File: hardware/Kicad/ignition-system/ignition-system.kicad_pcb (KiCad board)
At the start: 2 copper layers, 92 x 60.2 mm, 27 parts, among them J1 Screw_Terminal_01x02, SW1 SW_Push, SW2 SW_SPDT

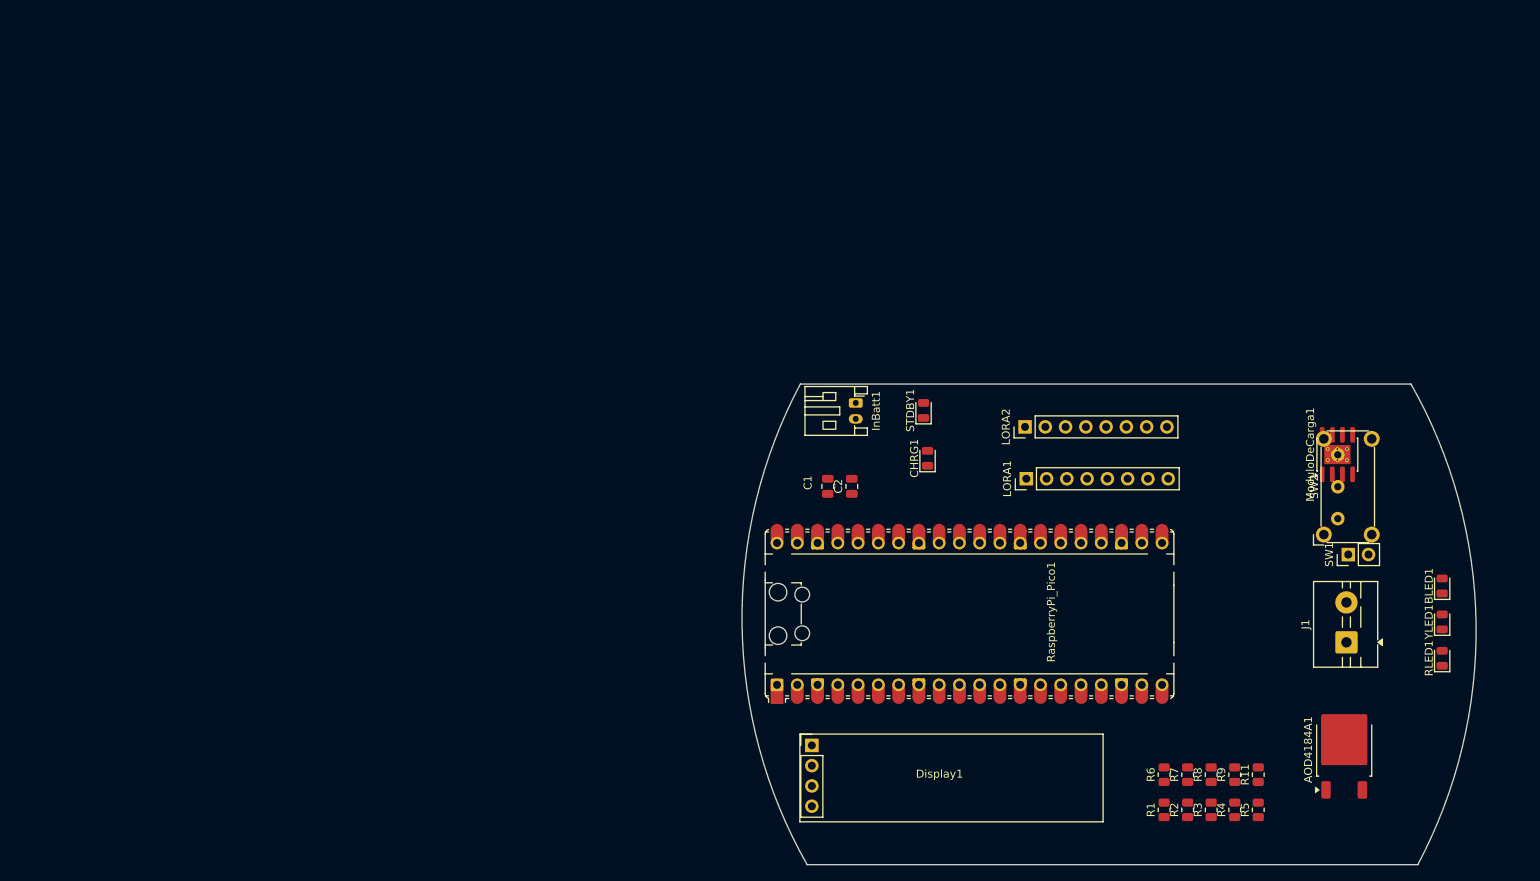
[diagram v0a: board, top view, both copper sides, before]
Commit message: feat: net class power, contorno 70x50 y placement completo
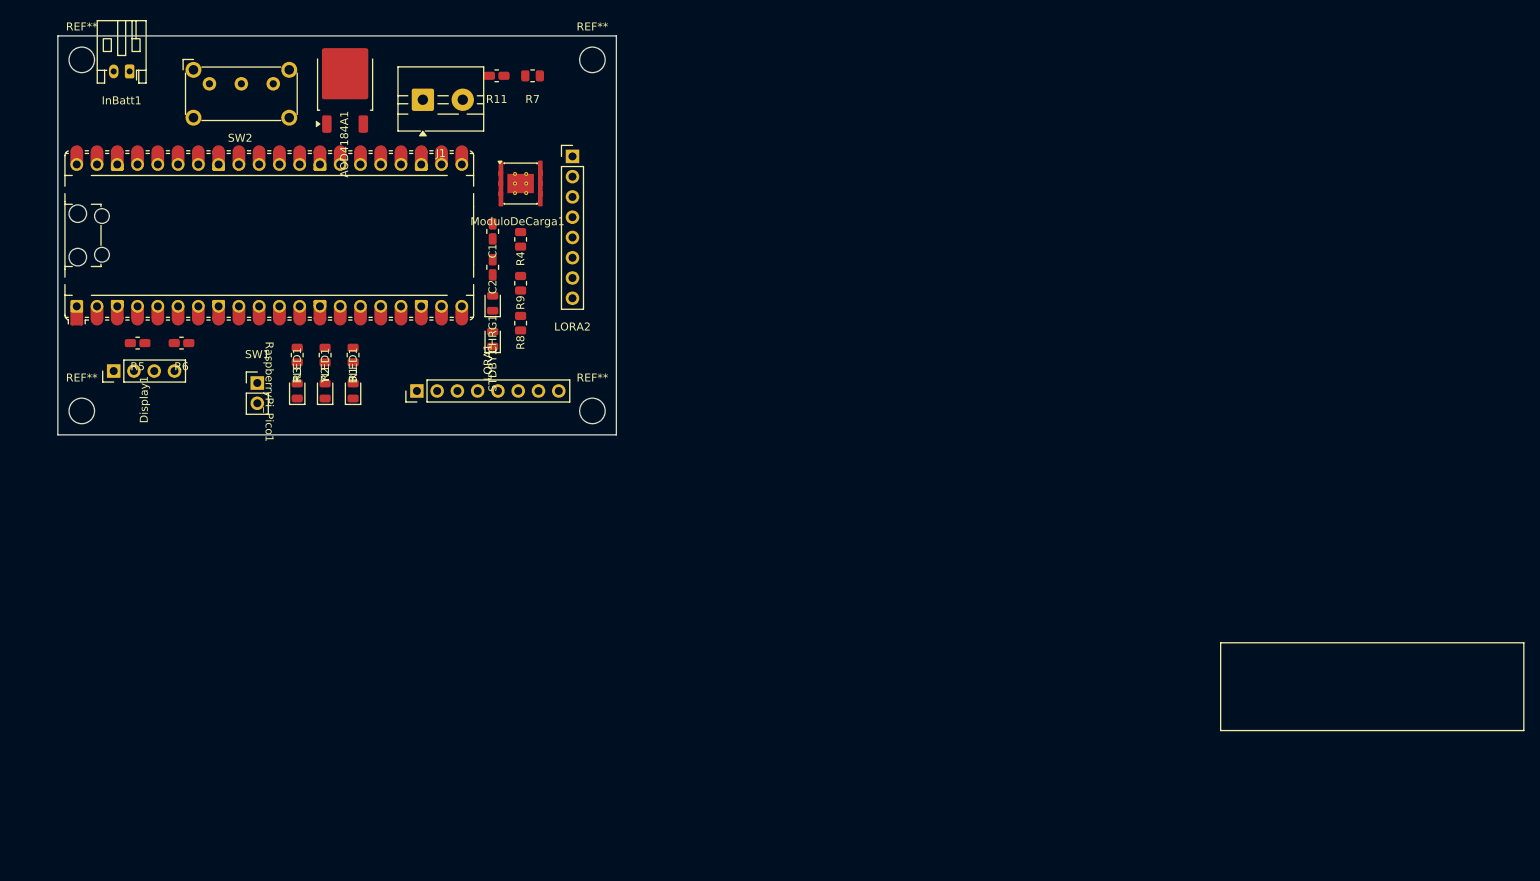
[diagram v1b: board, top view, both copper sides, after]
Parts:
- added REF**: MountingHole_3.2mm_M3, MountingHole:MountingHole_3.2mm_M3, F.Cu at (34.0, 33.0)
- added REF**: MountingHole_3.2mm_M3, MountingHole:MountingHole_3.2mm_M3, F.Cu at (98.0, 33.0)
- added REF**: MountingHole_3.2mm_M3, MountingHole:MountingHole_3.2mm_M3, F.Cu at (98.0, 77.0)
- added REF**: MountingHole_3.2mm_M3, MountingHole:MountingHole_3.2mm_M3, F.Cu at (34.0, 77.0)
- moved R5 152.1 mm to (41.0, 68.5), turned to 0 degrees
- moved SW2 151.6 mm to (50.0, 36.0), turned to 0 degrees
- moved AOD4184A1 150.5 mm to (67.0, 36.0)
- moved RLED1 147.4 mm to (61.0, 74.5)
- moved YLED1 143.0 mm to (64.5, 74.5)
- moved BLED1 138.7 mm to (68.0, 74.5)
- moved SW1 138.4 mm to (56.0, 73.5), turned to 0 degrees
- moved R6 134.5 mm to (46.5, 68.5), turned to 0 degrees
- moved J1 134.2 mm to (76.8, 38.0), turned to 0 degrees
- moved R11 129.5 mm to (86.0, 35.0), turned to 0 degrees
- moved R3 127.9 mm to (61.0, 70.0)
- moved R2 122.2 mm to (64.5, 70.0)
- moved R7 120.0 mm to (90.5, 35.0), turned to 0 degrees
- moved R1 116.5 mm to (68.0, 70.0)
- moved R4 114.6 mm to (89.0, 55.5)
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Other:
- board size 92 x 60.2 mm -> 70 x 50 mm

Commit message: fix: socket ra02 con gnd de bordes y ntc al temp
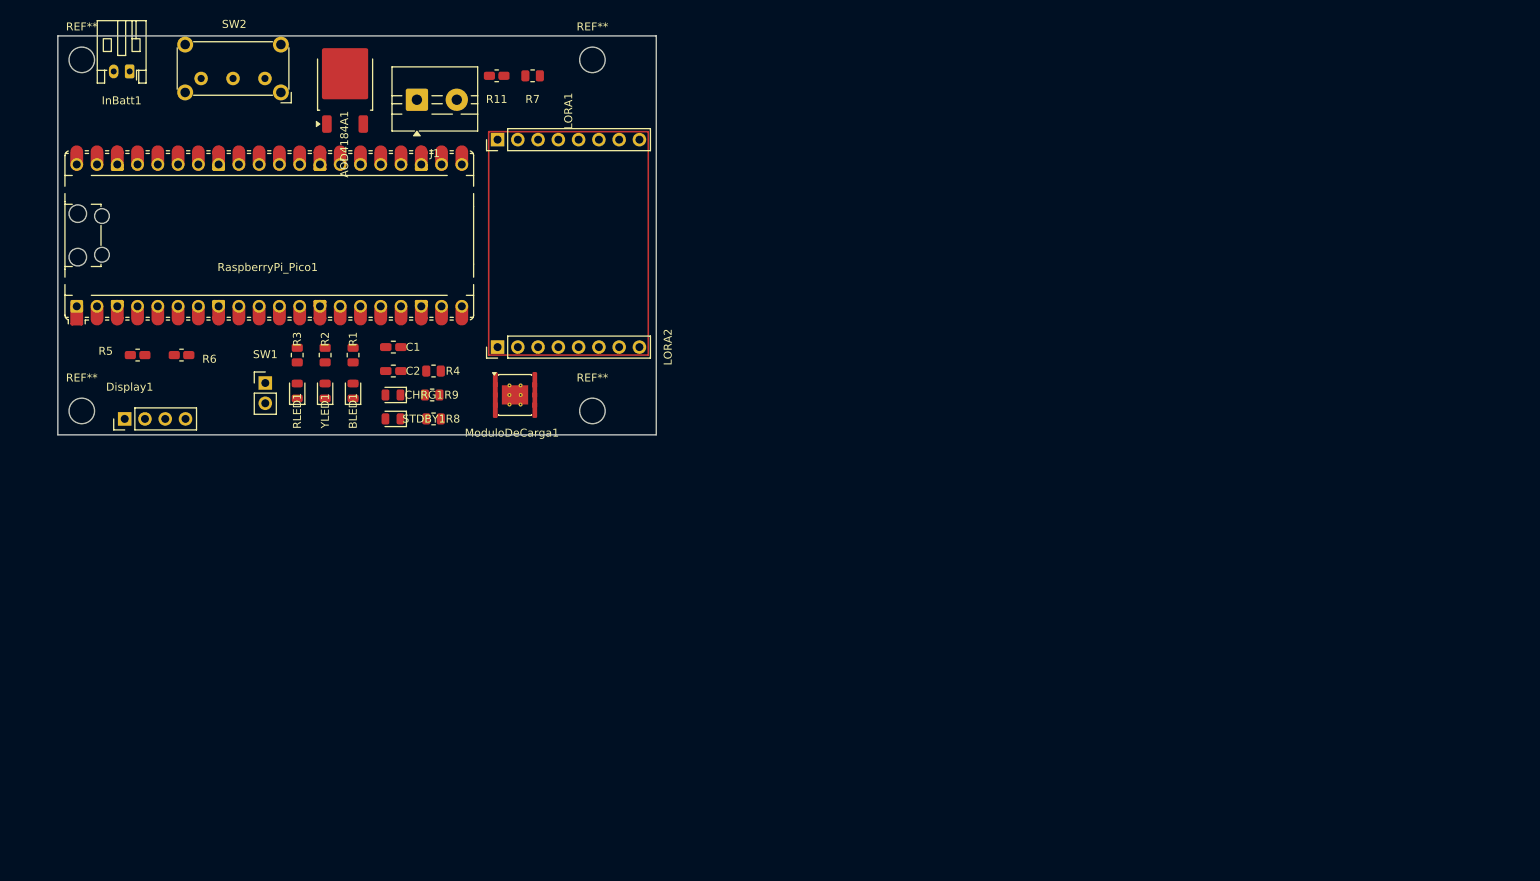
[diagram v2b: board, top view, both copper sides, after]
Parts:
- moved LORA1 33.1 mm to (86.1, 43.0)
- moved ModuloDeCarga1 26.5 mm to (88.3, 75.0)
- moved LORA2 25.7 mm to (86.1, 69.0), turned to 90 degrees
- moved R4 19.8 mm to (78.1, 72.0), turned to 180 degrees
- moved C1 19.1 mm to (73.0, 69.0), turned to 180 degrees
- moved C2 18.0 mm to (73.0, 72.0), turned to 180 degrees
- moved R9 17.9 mm to (77.9, 75.0), turned to 180 degrees
- moved CHRG1 17.0 mm to (73.0, 75.0), turned to 180 degrees
- moved R8 16.2 mm to (78.1, 78.0), turned to 180 degrees
- moved STDBY1 16.0 mm to (73.0, 78.0), turned to 180 degrees
- moved SW2 6.99 mm to (57.0, 35.3), turned to 180 degrees
- moved Display1 6.16 mm to (39.4, 78.0)
- moved R5 1.50 mm to (41.0, 70.0)
- moved R6 1.50 mm to (46.5, 70.0)
- moved SW1 1.00 mm to (57.0, 73.5)
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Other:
- board size 70 x 50 mm -> 75 x 50 mm

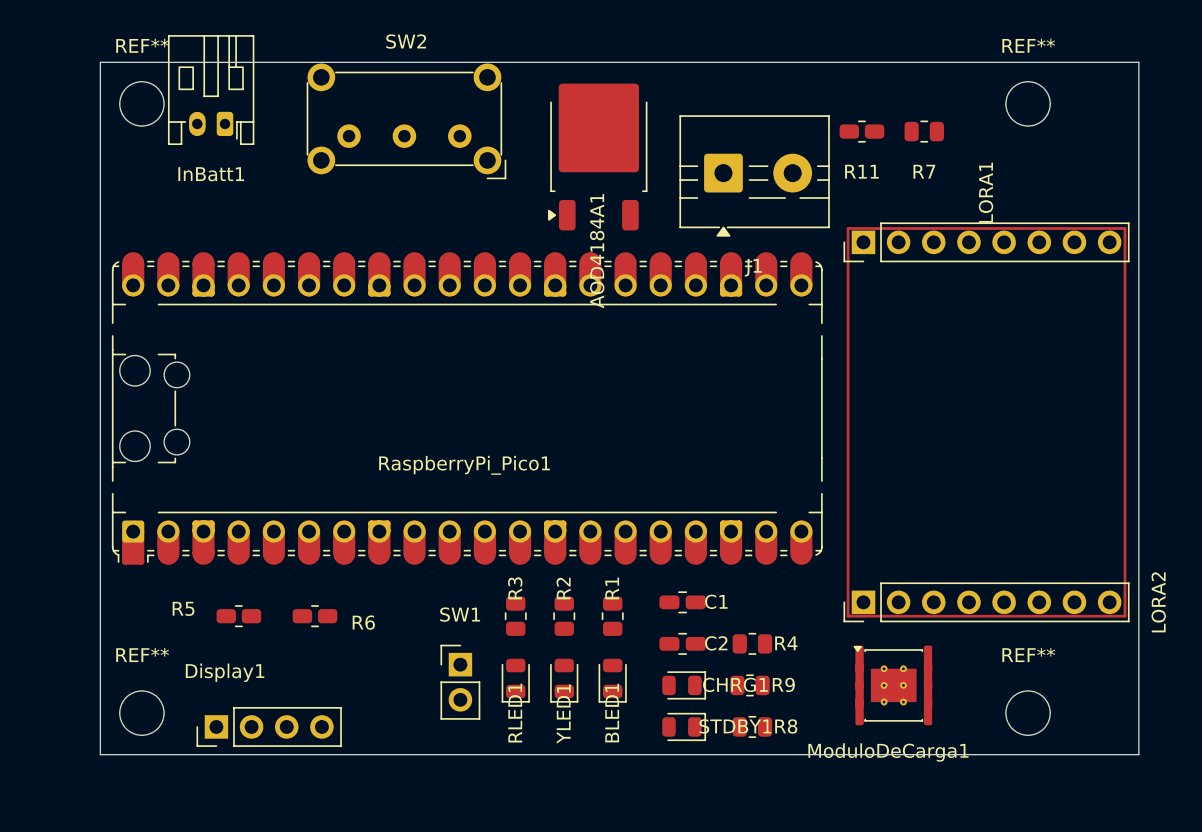
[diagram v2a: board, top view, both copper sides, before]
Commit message: feat: sw3 en consumo, tp4056 fijo a bateria, pwr flag de v
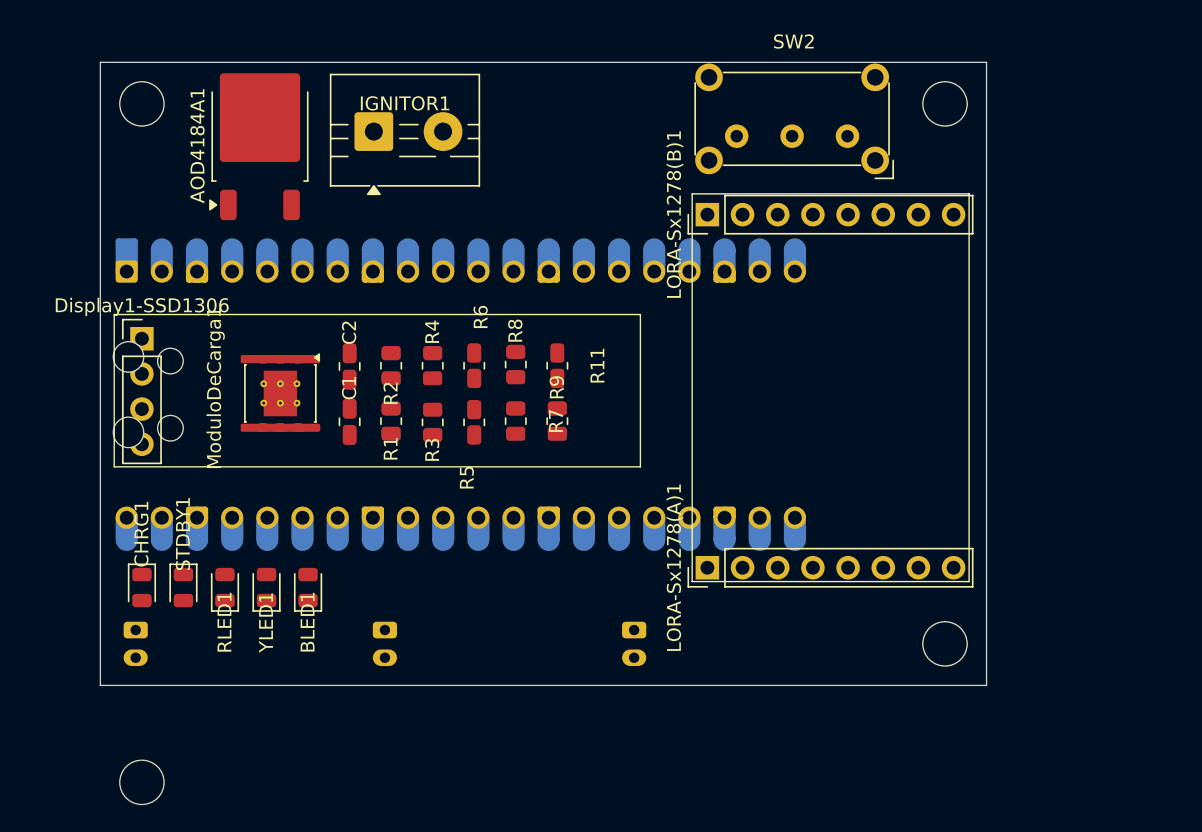
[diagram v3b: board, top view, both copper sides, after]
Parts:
- removed Display1: Conn_01x04, Connector_PinHeader_2.54mm:PinHeader_1x04_P2.54mm_Vertical
- removed J1: Screw_Terminal_01x02, TerminalBlock:TerminalBlock_MaiXu_MX126-5.0-02P_1x02_P5.00mm
- removed LORA1, LORA2: Conn_01x08, Connector_PinHeader_2.54mm:PinHeader_1x08_P2.54mm_Vertical
- removed RaspberryPi_Pico1: RaspberryPi_Pico, Module:RaspberryPi_Pico_Common_Unspecified
- added Display1-SSD1306: Conn_01x04, Connector_PinHeader_2.54mm:PinHeader_1x04_P2.54mm_Vertical, F.Cu at (34.0, 50.0)
- added IGNITOR1: Screw_Terminal_01x02, TerminalBlock:TerminalBlock_MaiXu_MX126-5.0-02P_1x02_P5.00mm, F.Cu at (50.8, 35.0)
- added LORA-Sx1278(A)1: Conn_01x08, Connector_PinHeader_2.54mm:PinHeader_1x08_P2.54mm_Vertical, F.Cu at (74.8, 66.5)
- added LORA-Sx1278(B)1: Conn_01x08, Connector_PinHeader_2.54mm:PinHeader_1x08_P2.54mm_Vertical, F.Cu at (74.8, 41.0)
- added RaspberryPi_Pico1-RP2040: RaspberryPi_Pico, Module:RaspberryPi_Pico_Common_Unspecified, B.Cu at (57.0, 54.0)
- added TH1: NTC 10k B3950, Connector_JST:JST_PH_S2B-PH-K_1x02_P2.00mm_Horizontal, B.Cu at (51.5, 71.0)
- InBatt1: moved to B.Cu
- SW1: footprint Connector_PinHeader_2.54mm:PinHeader_1x02_P2.54mm_Vertical -> Connector_JST:JST_PH_S2B-PH-K_1x02_P2.00mm_Horizontal; moved to B.Cu
- moved ModuloDeCarga1 49.1 mm to (44.0, 53.9), turned to -90 degrees
- moved CHRG1 39.6 mm to (34.0, 67.9), turned to -90 degrees
- moved STDBY1 37.4 mm to (37.0, 67.9), turned to -90 degrees
- moved InBatt1 37.1 mm to (33.5, 71.0), turned to -90 degrees
- moved R7 36.2 mm to (61.0, 55.9), turned to 90 degrees
- moved C2 31.3 mm to (49.0, 52.0), turned to -90 degrees
- moved R8 31.3 mm to (61.0, 51.8), turned to -90 degrees
- moved R4 30.6 mm to (55.0, 51.9), turned to -90 degrees
- moved SW2 28.0 mm to (85.0, 35.3)
- moved R11 27.7 mm to (64.0, 51.9), turned to 90 degrees
- moved C1 27.4 mm to (49.0, 56.0), turned to -90 degrees
- moved AOD4184A1 24.5 mm to (42.5, 35.3)
- moved R9 23.6 mm to (64.0, 55.9), turned to -90 degrees
- moved BLED1 23.0 mm to (46.0, 67.9)
- moved YLED1 22.5 mm to (43.0, 67.9)
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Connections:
- ModuloDeCarga1 pad 1: GND -> Net-(ModuloDeCarga1-TEMP)
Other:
- board size 75 x 50 mm -> 64 x 45 mm

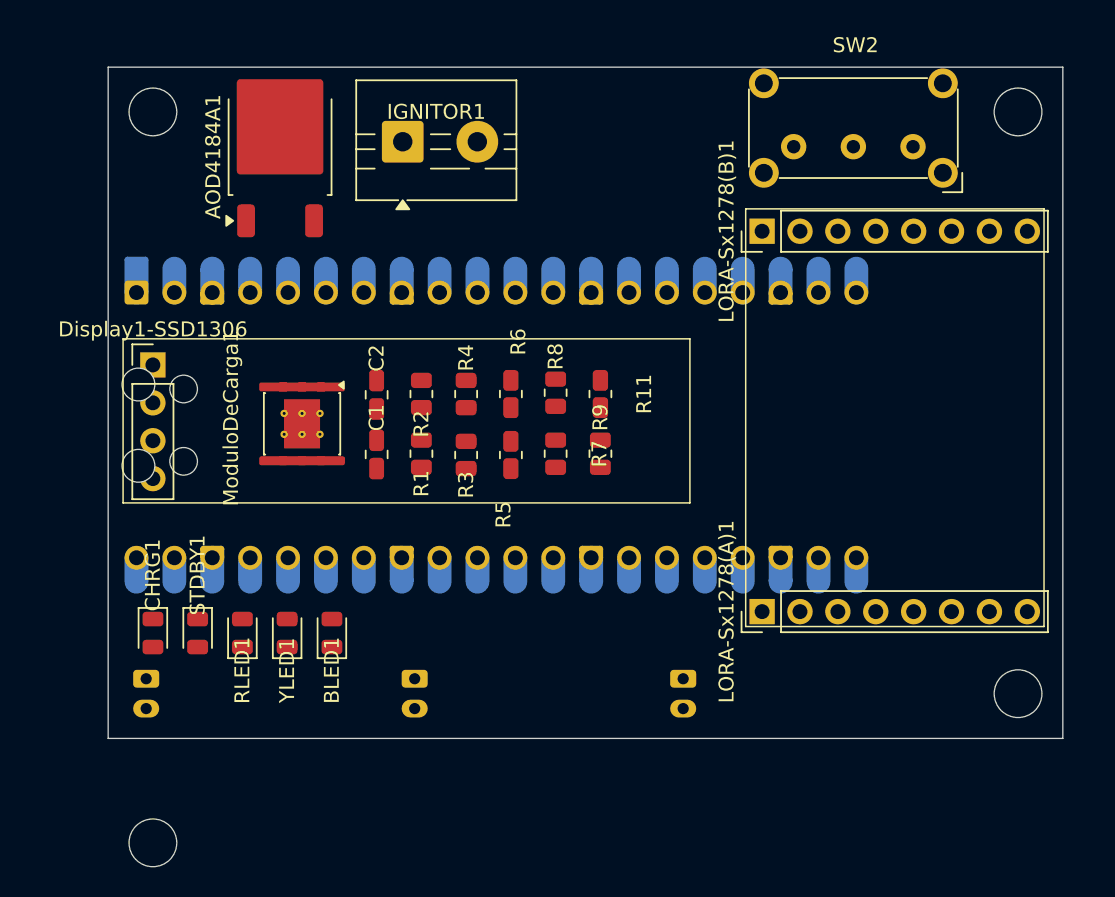
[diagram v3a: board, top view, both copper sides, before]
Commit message: feat: ruteo pcb de ignition-system
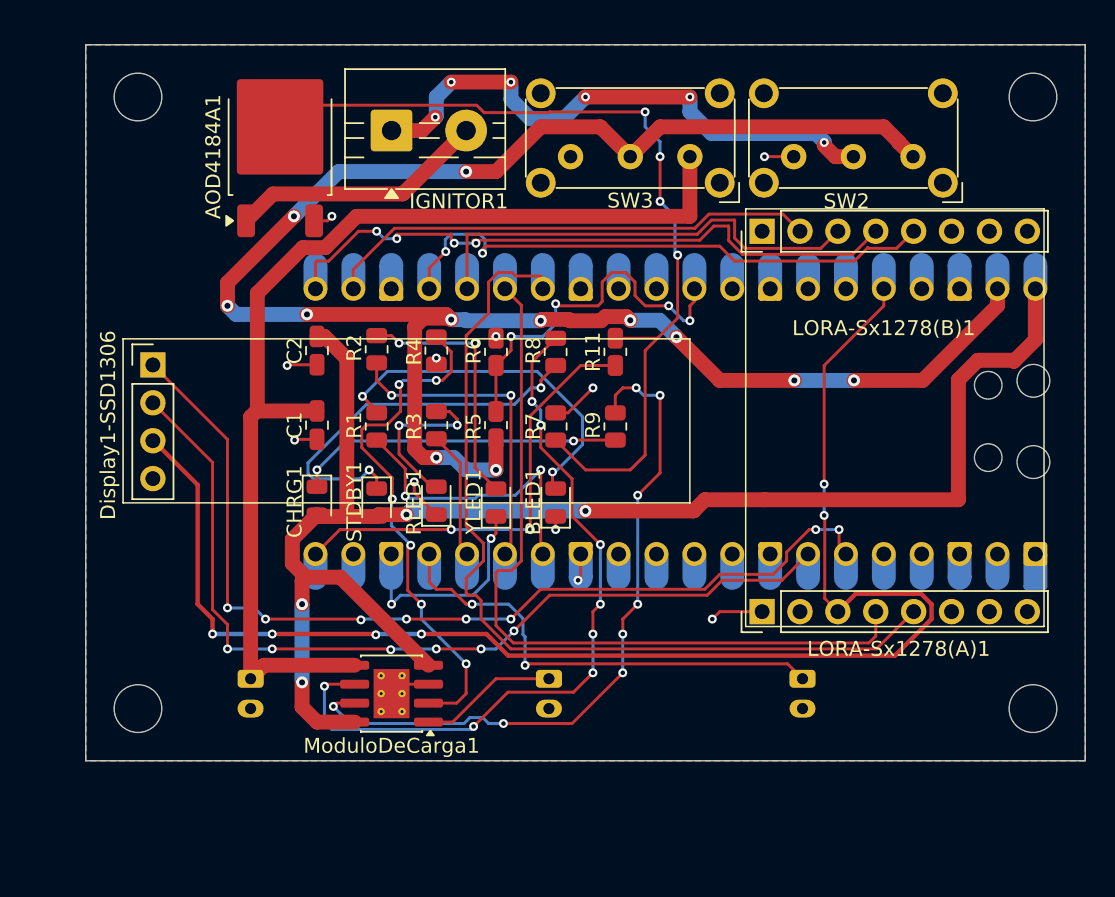
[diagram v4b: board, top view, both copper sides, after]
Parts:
- added SW3: SW_SPDT, Button_Switch_THT:SW_E-Switch_EG1224_SPDT_Angled, F.Cu at (70.0, 36.0)
- moved ModuloDeCarga1 19.1 mm to (50.0, 72.0), turned to 180 degrees
- moved BLED1 17.4 mm to (61.0, 59.2)
- moved YLED1 16.5 mm to (57.0, 59.2)
- moved RLED1 15.7 mm to (53.0, 59.1)
- moved STDBY1 14.9 mm to (49.0, 59.2)
- moved CHRG1 14.1 mm to (45.0, 59.1)
- moved RaspberryPi_Pico1-RP2040 12.0 mm to (69.0, 53.8), turned to 90 degrees
- moved REF** 9.06 mm to (33.0, 73.0)
- moved TH1 9.00 mm to (60.5, 71.0)
- moved SW1 8.00 mm to (77.5, 71.0)
- moved InBatt1 7.00 mm to (40.5, 71.0)
- moved C2 4.98 mm to (45.0, 49.0)
- moved C1 4.46 mm to (45.0, 54.0)
- moved R2 4.24 mm to (49.0, 48.9)
- moved R4 3.53 mm to (53.0, 49.0)
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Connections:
- C1 pad 1: VSYS -> Net-(InBatt1-Pin_1)
- InBatt1 pad 1: VSYS -> Net-(InBatt1-Pin_1)
- ModuloDeCarga1 pad 5: VSYS -> Net-(InBatt1-Pin_1)
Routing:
- net VSYS: track 0.00 -> 130.6 mm, vias 0 -> 12
- net VBUS: track 0.00 -> 103.1 mm, vias 0 -> 4
- net 3V3: track 0.00 -> 96.3 mm, vias 0 -> 6
- net Net-(InBatt1-Pin_1): track 0.00 -> 72.5 mm
- net SDA: track 0.00 -> 64.6 mm, vias 0 -> 8
- net DIO0: track 0.00 -> 60.5 mm
- net Net-(AOD4184A1-G): track 0.00 -> 60.2 mm, vias 0 -> 4
- net SCL: track 0.00 -> 60.2 mm, vias 0 -> 6
- net RST: track 0.00 -> 52.0 mm
- net STDBY: track 0.00 -> 49.5 mm, vias 0 -> 8
- net CHRG: track 0.00 -> 47.4 mm, vias 0 -> 8
- net MISO: track 0.00 -> 44.2 mm, vias 0 -> 4
- net SCK: track 0.00 -> 38.5 mm, vias 0 -> 2
- net Net-(IGNITOR1-Pin_1): track 0.00 -> 37.5 mm, vias 0 -> 6
- net GND: track 0.00 -> 37.3 mm, vias 0 -> 13
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- added copper zone on B.Cu, net GND
- added copper zone on F.Cu, net GND
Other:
- board size 64 x 45 mm -> 67 x 48 mm
